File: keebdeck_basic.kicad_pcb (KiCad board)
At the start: 2 copper layers, 87.4 x 67.6 mm, 120 parts, among them J1 USB_C_Receptacle_USB2.0, J2 Conn_Qwiic, SW1 SW_ESC, SW10 SW_1, SW11 SW_2, SW12 SW_3, SW13 SW_4, SW14 SW_5, SW15 SW_6, SW16 SW_7, SW17 SW_8, SW18 SW_9, SW19 SW_0, SW2 SW_SQUARE, SW20 SW_-, SW21 SW_=, SW22 SW_TAB, SW23 SW_Q, SW24 SW_W, SW25 SW_E, SW26 SW_R, SW27 SW_T, SW28 SW_Y, SW29 SW_U, SW3 SW_TRIANGLE, SW30 SW_I, SW31 SW_O, SW32 SW_P, SW33 SW_[, SW34 SW_], SW35 SW_FN, SW36 SW_A, SW37 SW_S, SW38 SW_D, SW39 SW_F, SW4 SW_CROSS, SW40 SW_G, SW41 SW_H, SW42 SW_J, SW43 SW_K, SW44 SW_L, SW45 SW_;, SW46 SW_', SW47 SW_ENTER, SW48 SW_LSHIFT, SW49 SW_Z, SW5 SW_CIRCLE, SW50 SW_X, SW51 SW_C, SW52 SW_V, SW53 SW_B, SW54 SW_N, SW55 SW_M, SW56 SW_,, SW57 SW_., SW58 SW_/, SW59 SW_UP, SW6 SW_CLUB, SW60 SW_RSHIFT, SW61 SW_CTRL, SW62 SW_SP, SW63 SW_LALT, SW64 SW_\, SW65 SW_SPACE1, SW66 SW_SPACE2, SW67 SW_SPACE3, SW68 SW_RALT, SW69 SW_LEFT, SW7 SW_DIAMOND, SW70 SW_DOWN, SW71 SW_RIGHT, SW72 SW_BOOT, SW8 SW_BACKSPACE, SW9 SW_TILDE, U1 AP3032KTR, U2 AP2112K-3.3, U3 STM32F042G6Ux

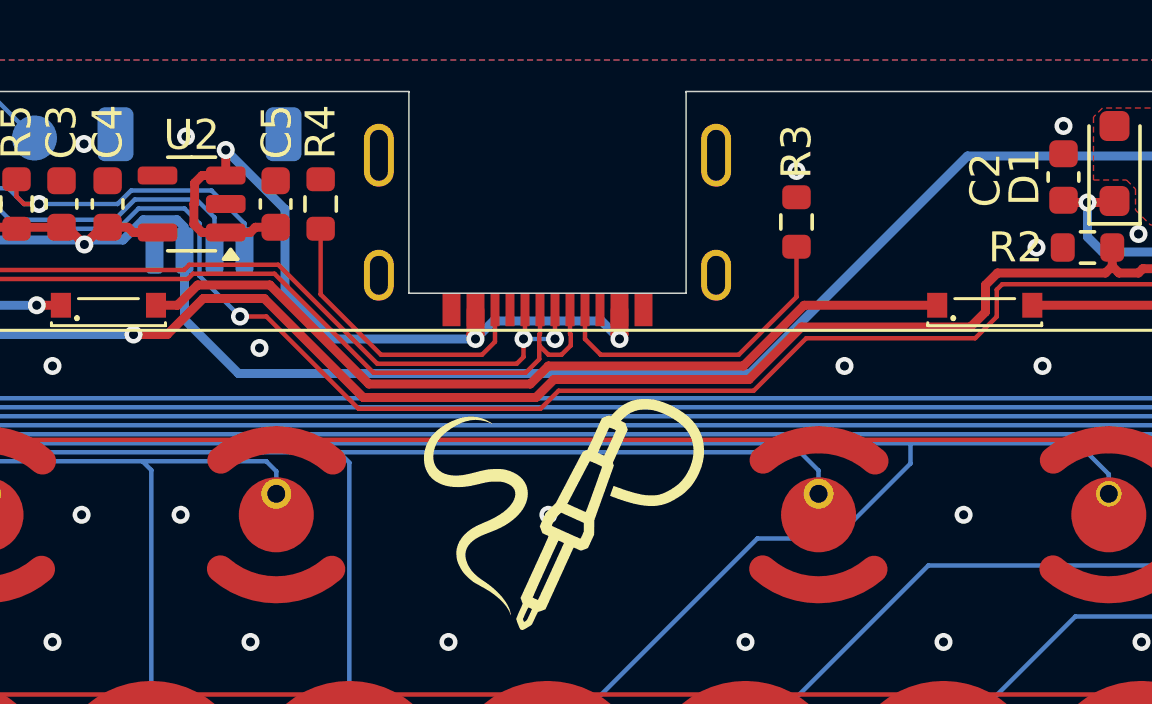
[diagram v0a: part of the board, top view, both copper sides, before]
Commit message: Efficiency and EMI improvements
Changed the voltage supply for the backlight from +3.3V to +5V. This should improve the power efficiency slightly, as the AP3032 is more efficient at 5V input, and the LDO needs to handle less current.

Also added vias next to the GND pads of the USB-C connector, this might slightly improve EMI at no extra costs.
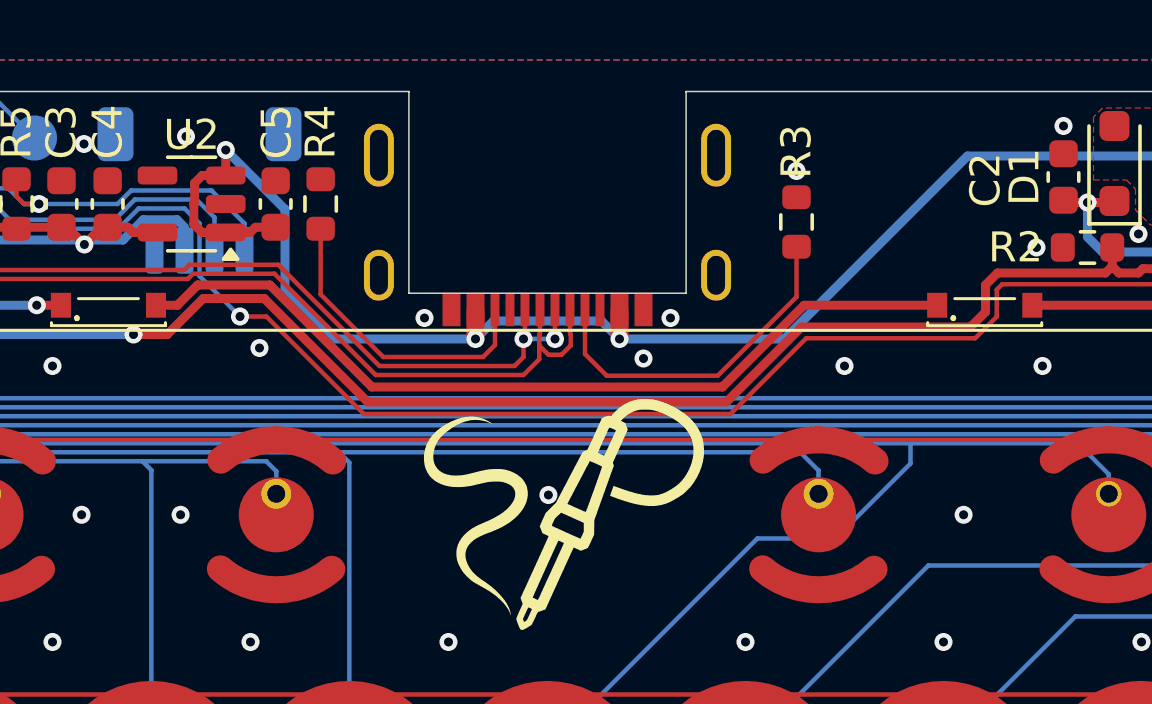
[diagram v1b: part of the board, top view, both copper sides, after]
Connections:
- C1 pad 1: +3.3V -> +5V
- L1 pad 1: +3.3V -> +5V
- U1 pad 6: +3.3V -> +5V
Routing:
- net +3.3V: track 79.3 -> 36.8 mm, vias 3 -> 2
- net +5V: track 28.3 -> 52.7 mm, vias 3 -> 4
- net Net-(J1-CC1): track 10.7 -> 11.6 mm
- net GND: vias 157 -> 160
- added copper zone on F.Cu, net +5V
- removed copper zone on F.Cu, net +3.3V
